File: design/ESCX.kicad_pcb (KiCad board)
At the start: 4 copper layers, 100 x 90 mm, 138 parts, among them J1 SWD, J2 Conn_Coaxial, J3 Screw_Terminal_01x02, J4 Screw_Terminal_01x03, J5 HALL_ENC, J6 USB_C_Receptacle_USB2.0_16P, Q1 IRF7854, Q2 IRF7854, Q3 IRF7854, Q4 IRF7854, Q5 IRF7854, Q6 IRF7854, SW1 SENSOR_VOLTAGE, U1 STM32F40X_LQFP64, U2 LM3671, U3 DRV8301, U4 nRF24L01P, U5 AD8418, U6 AD8418, U7 AD8418, X1 8MHz, X2 16MHz

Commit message: Correccion de DRC
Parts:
- J2: footprint Connector_Coaxial:SMA_Amphenol_901-143_Horizontal -> Connector_Coaxial:SMA_Amphenol_901-144_Vertical
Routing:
- net +3.3V: track 121.7 -> 116.0 mm

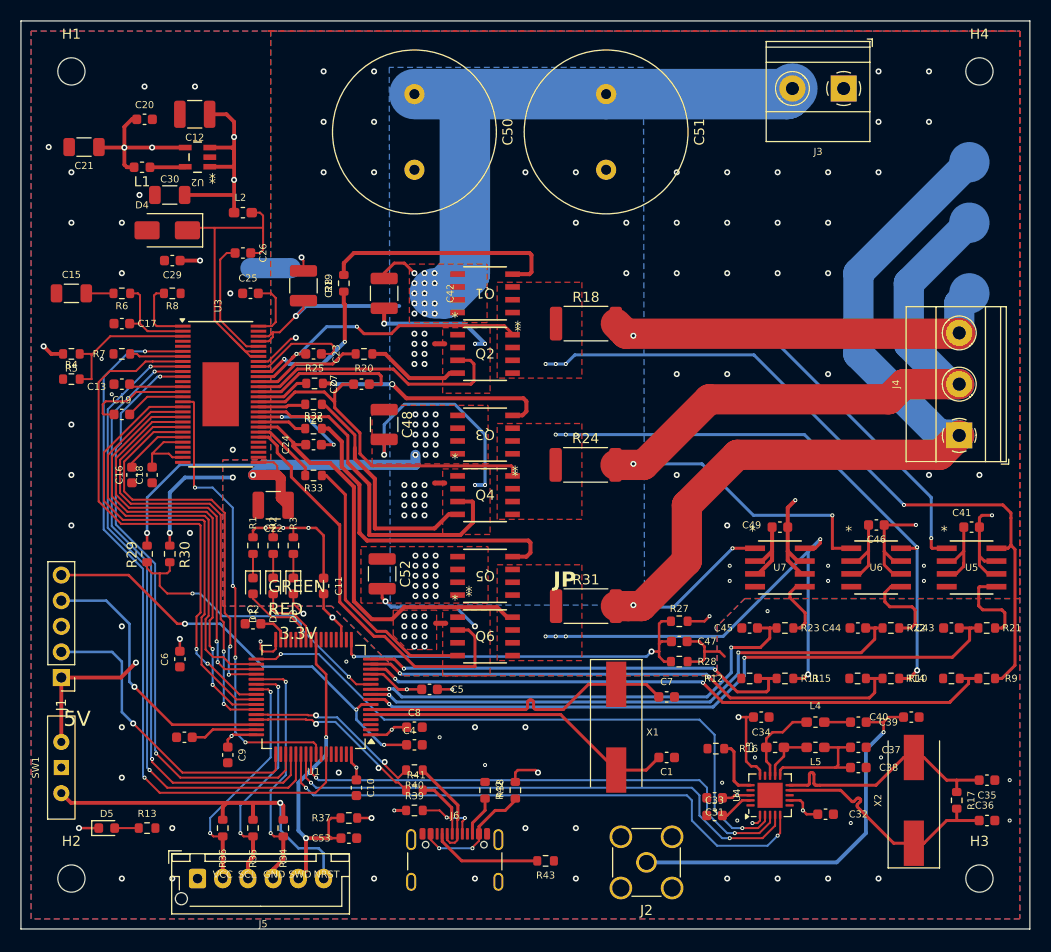
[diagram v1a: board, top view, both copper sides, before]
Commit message: reubicacion de designadores de Silkscreen
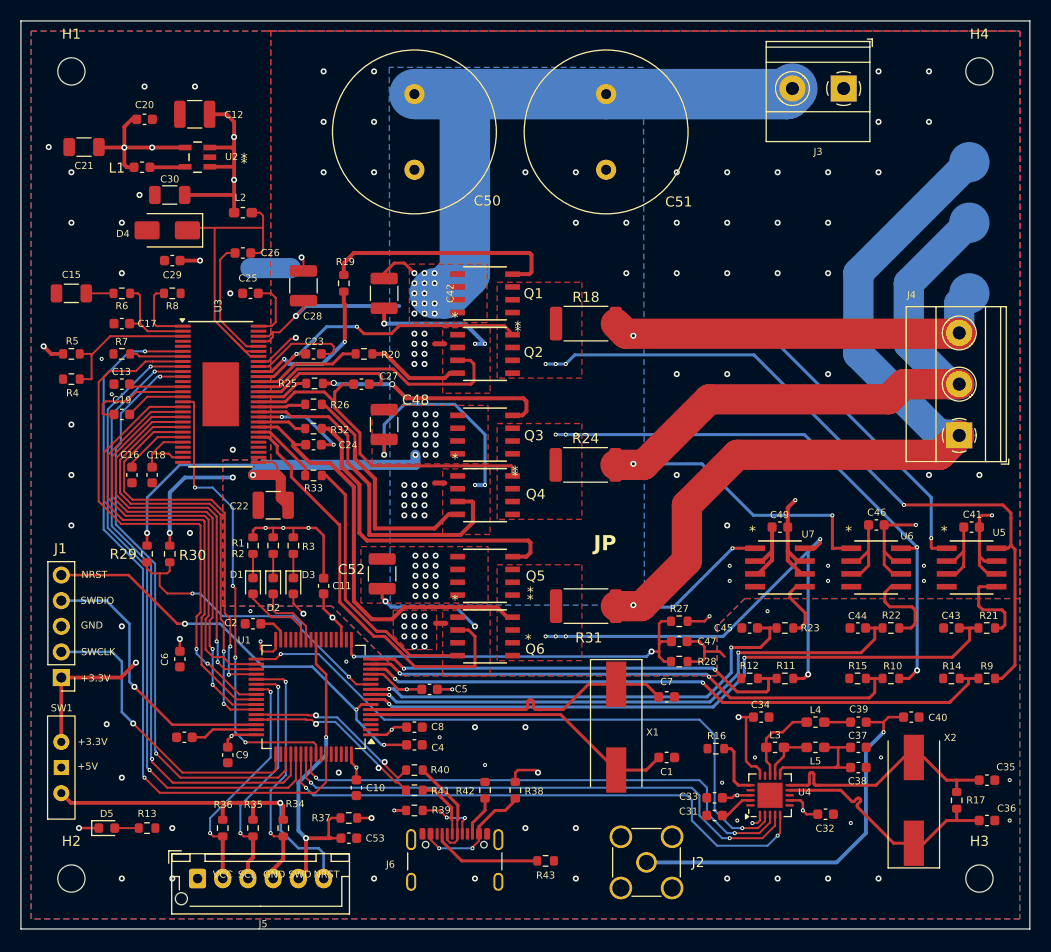
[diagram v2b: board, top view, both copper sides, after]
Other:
- board text added: "+3.3V"
- board text added: "+5V"
- board text added: "SWCLK"
- board text added: "SWDIO"
- board text removed: "3.3V"
- board text removed: "5V"
- board text removed: "GREEN"
- board text removed: "RED"

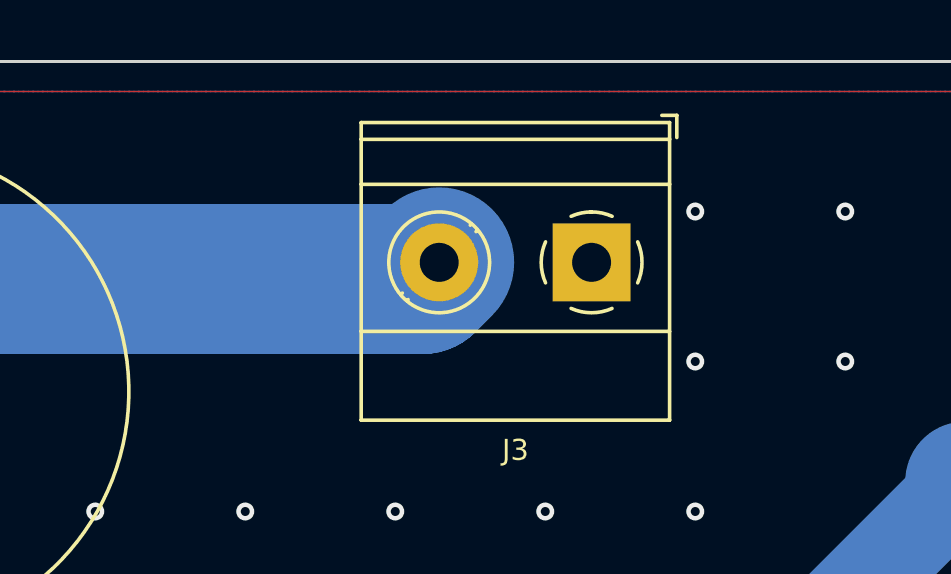
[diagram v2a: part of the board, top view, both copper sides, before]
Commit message: Agrego texto con +supply
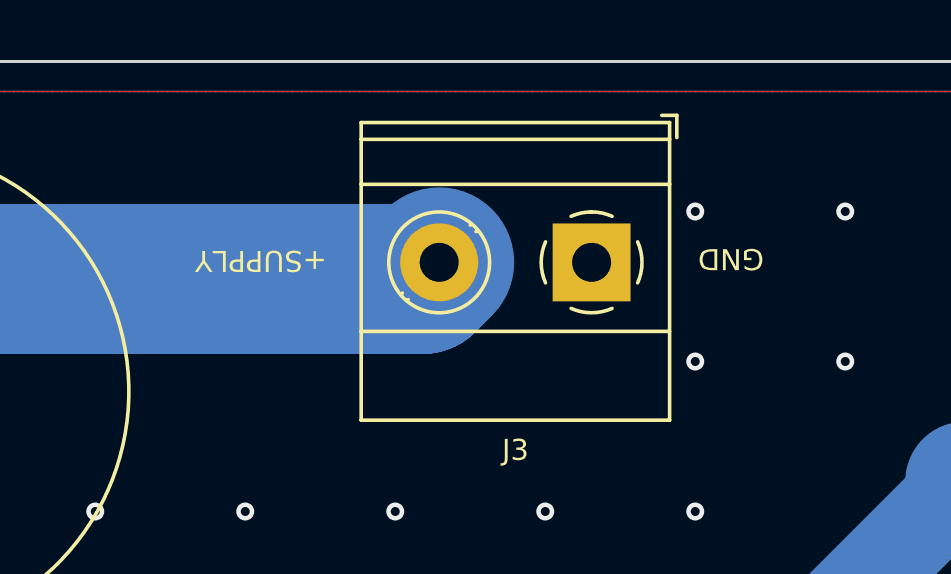
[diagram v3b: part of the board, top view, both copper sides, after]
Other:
- board text added: "+SUPPLY"
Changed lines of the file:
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@@
+		)
+	)
+	(gr_text "GND"
+		(at 185.19 50.58 180)
+		(layer "F.SilkS")
+		(effects
+			(font
+				(size 0.7 0.7)
+				(thickness 0.1)
+			)
 		)
 	)
@@
 		(layer "F.SilkS")
 		(effects
+			(font
+				(size 0.7 0.7)
+				(thickness 0.1)
+			)
+		)
+	)
+	(gr_text "+SUPPLY"
+		(at 169.52 50.64 180)
+		(layer "F.SilkS")
+		(effects

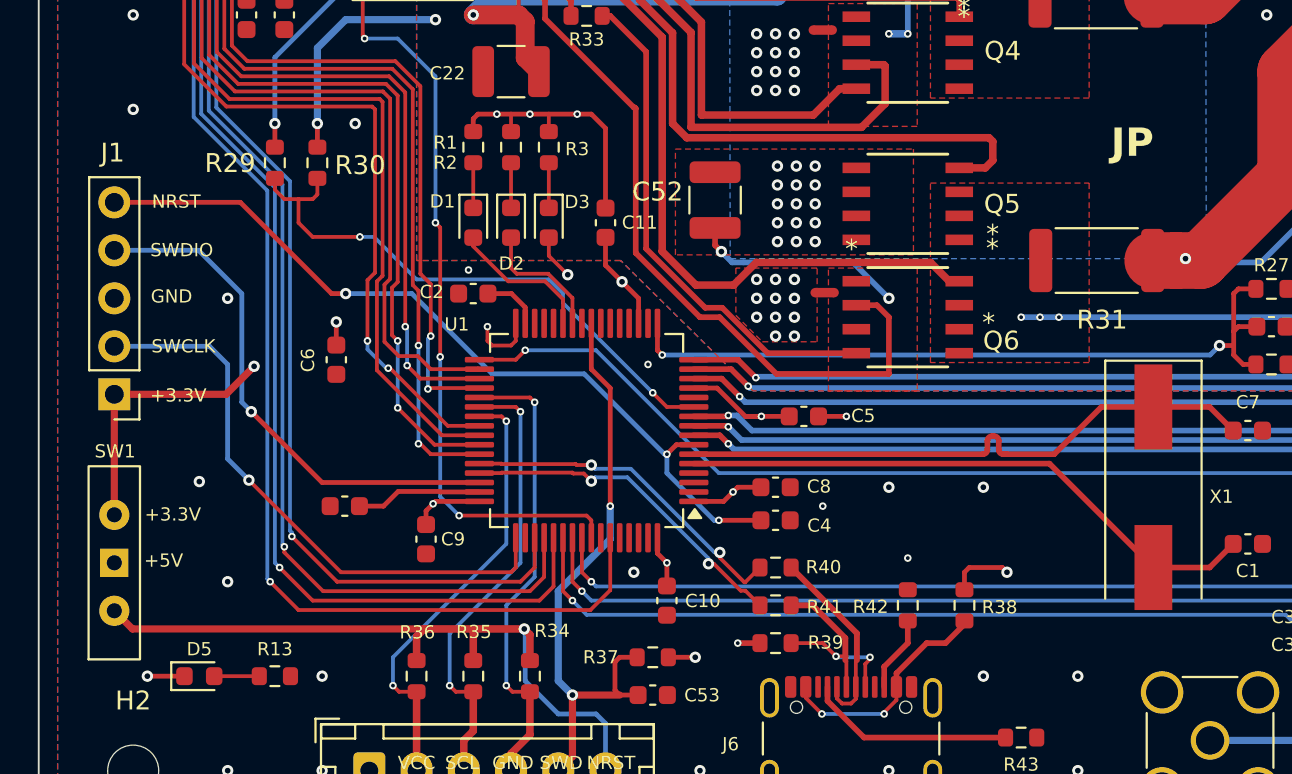
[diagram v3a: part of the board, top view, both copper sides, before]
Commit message: Cambio de switch de tension del sensor por jumper
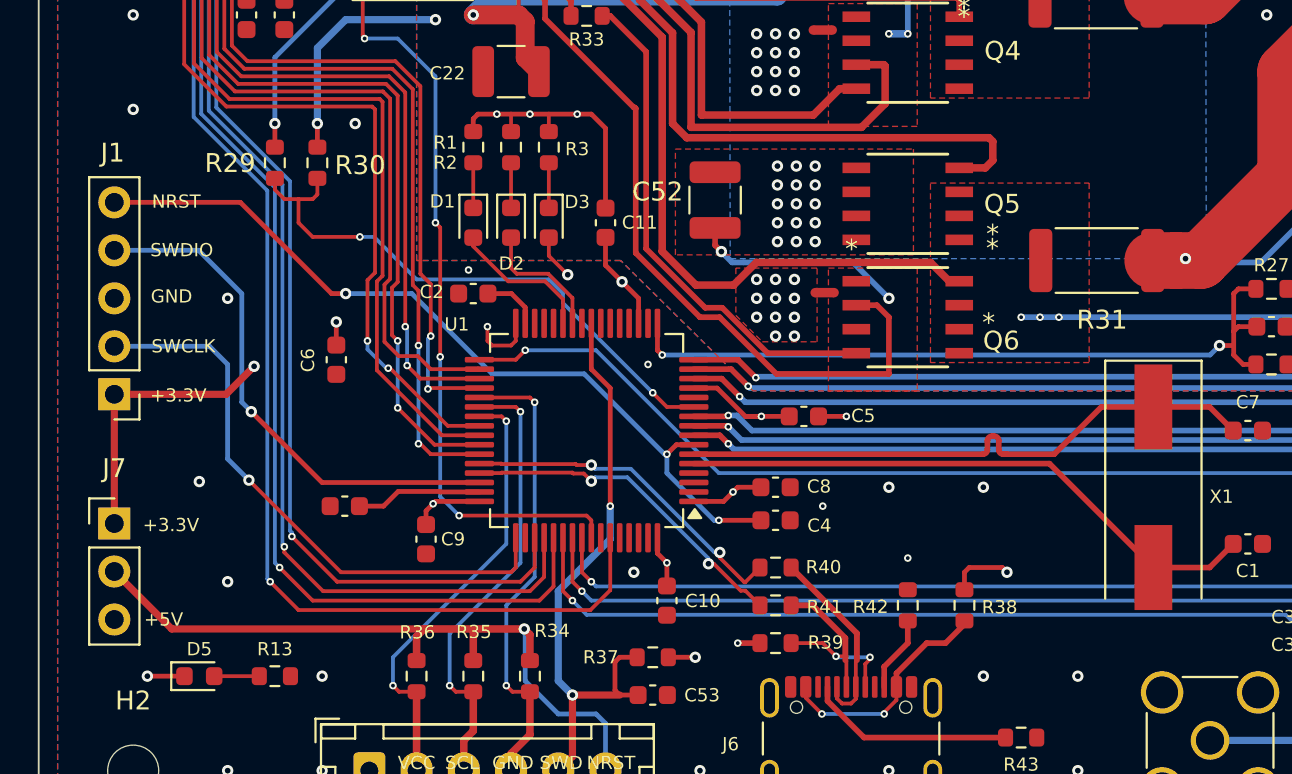
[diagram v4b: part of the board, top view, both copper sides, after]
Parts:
- removed SW1: SENSOR_VOLTAGE, Button_Switch_THT:SW_Slide-03_Wuerth-WS-SLTV_10x2.5x6.4_P2.54mm
- added J7: Sensor Voltage Switch, Connector_PinHeader_2.54mm:PinHeader_1x03_P2.54mm_Vertical, F.Cu at (103.0, 115.9)
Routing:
- net Net-(J5-Pin_6): track 37.9 -> 38.7 mm

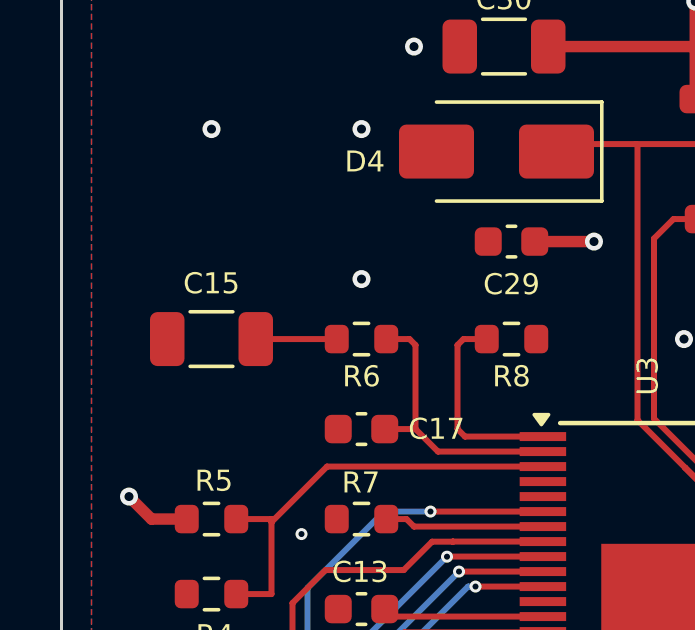
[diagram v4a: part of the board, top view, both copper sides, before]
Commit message: Abaratando costos
Cambios en numeros de jlcpcb, pasados a componentes básicos
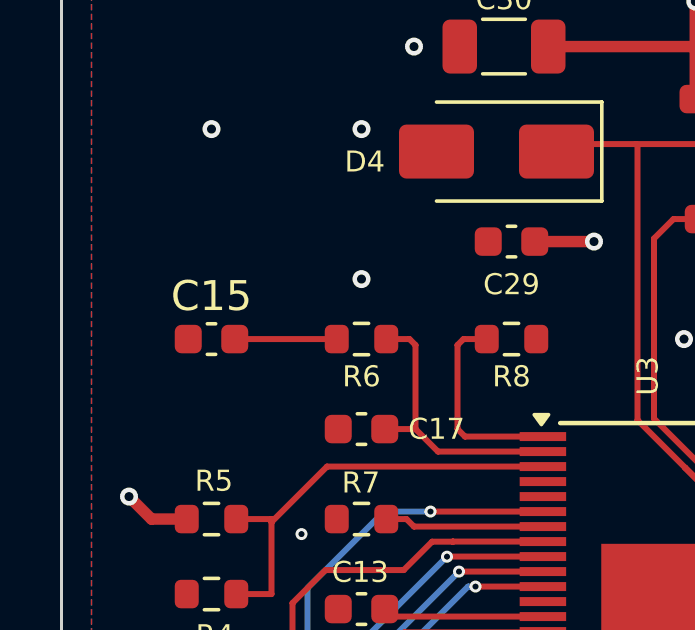
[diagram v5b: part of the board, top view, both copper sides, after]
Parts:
- C15: footprint Capacitor_SMD:C_1206_3216Metric -> Capacitor_SMD:C_0603_1608Metric
- D1: value Red LED -> R2
- D2: value Green LED -> G1
- D3: value Blue LED -> B3
- D5: value Red LED -> R4
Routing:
- net Net-(C15-Pad2): track 2.70 -> 3.40 mm

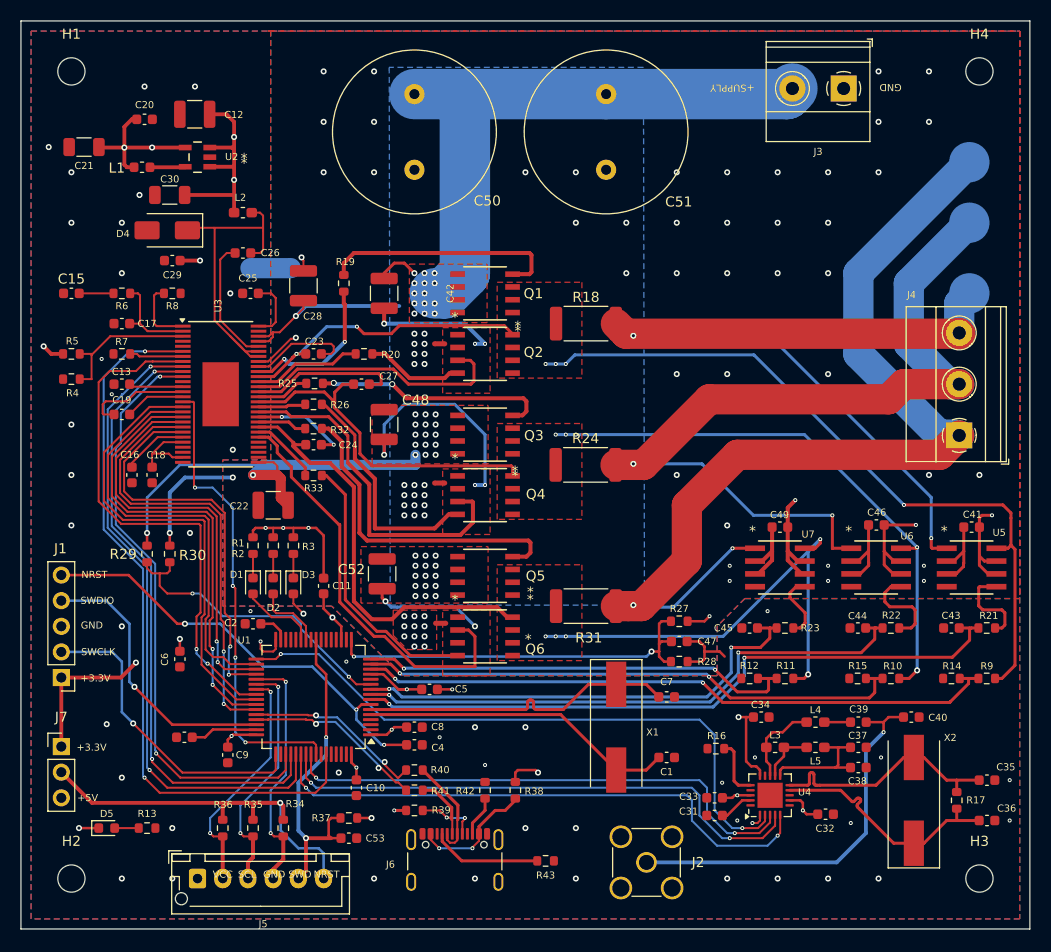
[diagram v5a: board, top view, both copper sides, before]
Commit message: Sacado de NRF
Sacado de NRF, re-hecho constraints
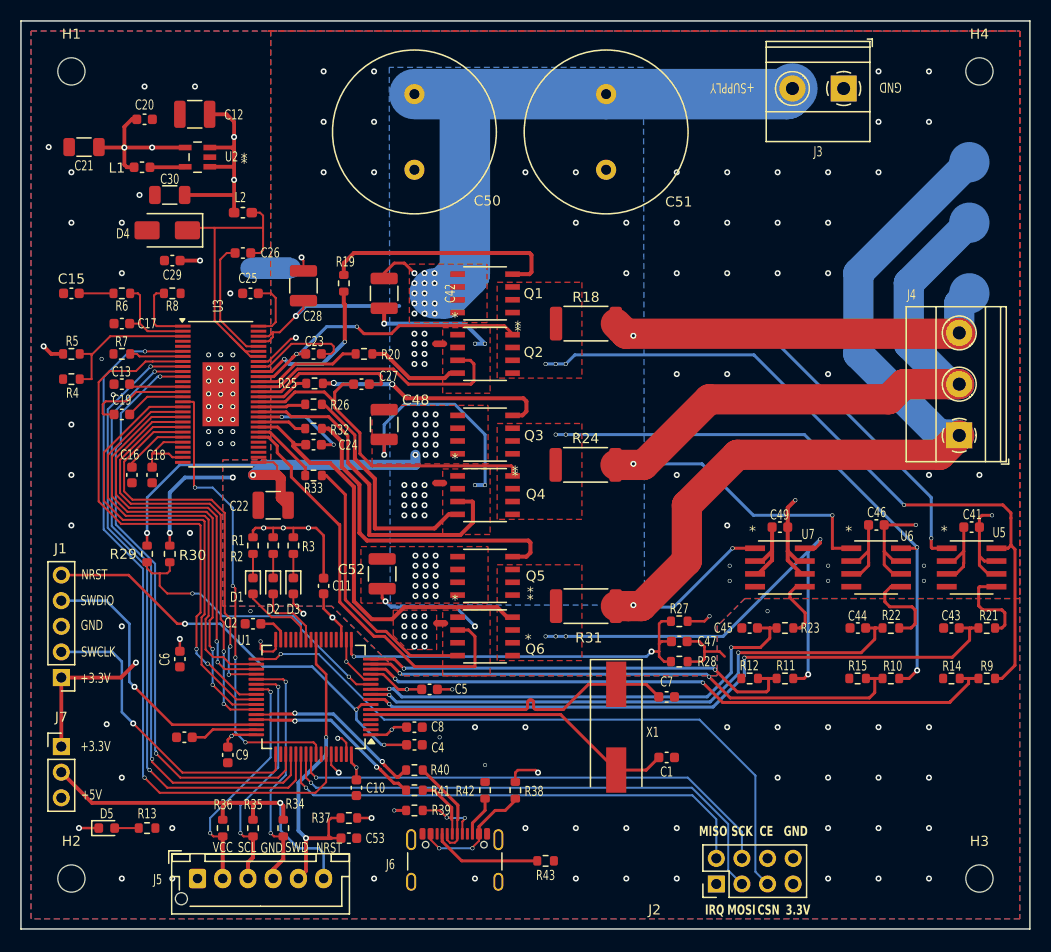
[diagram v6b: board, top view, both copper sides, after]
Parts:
- removed C31, C32, C33, C34: 100nF, Capacitor_SMD:C_0603_1608Metric
- removed C35, C36: 22pF, Capacitor_SMD:C_0603_1608Metric
- removed C37: 2.2nF, Capacitor_SMD:C_0603_1608Metric
- removed C38: 4.7pF, Capacitor_SMD:C_0603_1608Metric
- removed C39: 1.5pF, Capacitor_SMD:C_0603_1608Metric
- removed C40: 1pF, Capacitor_SMD:C_0603_1608Metric
- removed L3: 8.2n, Inductor_SMD:L_0603_1608Metric_Pad1.05x0.95mm_HandSolder
- removed L4: 3.9n, Inductor_SMD:L_0603_1608Metric_Pad1.05x0.95mm_HandSolder
- removed L5: 2.7n, Inductor_SMD:L_0603_1608Metric_Pad1.05x0.95mm_HandSolder
- removed R16: 22kΩ, Resistor_SMD:R_0603_1608Metric
- removed R17: 1MΩ, Resistor_SMD:R_0603_1608Metric
- removed U4: nRF24L01P, Package_DFN_QFN:QFN-20-1EP_4x4mm_P0.5mm_EP2.5x2.5mm
- removed X2: 16MHz, Crystal:Crystal_SMD_HC49-SD
- J2: value Conn_Coaxial -> Conn_02x04_Top_Bottom; footprint Connector_Coaxial:SMA_Amphenol_901-144_Vertical -> Connector_PinHeader_2.54mm:PinHeader_2x04_P2.54mm_Vertical
- moved J2 7.24 mm to (167.9, 129.5), turned to 90 degrees
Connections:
- J2 pad 1: Net-(J2-In) -> /NRF/IRQ
- J2 pad 2: GND1 -> /MCU/PD2
- J6 pad A6: /USB_Interface/dusb+ -> Net-(J6-D+-PadA6)
- J6 pad A7: /USB_Interface/dusb- -> Net-(J6-D--PadA7)
- J6 pad B6: /USB_Interface/dusb+ -> Net-(J6-D+-PadA6)
- J6 pad B7: /USB_Interface/dusb- -> Net-(J6-D--PadA7)
- R39 pad 2: /USB_Interface/dusb+ -> Net-(J6-D+-PadA6)
- R40 pad 1: /MCU/USB_DN -> /USB_Interface/dusb-
- R40 pad 2: /USB_Interface/dusb- -> Net-(J6-D--PadA7)
- R41 pad 1: /MCU/USB_DP -> /USB_Interface/dusb+
- R41 pad 2: /USB_Interface/dusb+ -> Net-(J6-D+-PadA6)
- U1 pad 44: /MCU/USB_DN -> /USB_Interface/dusb-
- U1 pad 45: /MCU/USB_DP -> /USB_Interface/dusb+
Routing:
- net Net-(J2-In): track 38.8 -> 0.00 mm, vias 1 -> 0
- net Net-(U4-XC2): track 24.2 -> 0.00 mm
- net Net-(U4-XC1): track 24.2 -> 0.00 mm
- net /MCU/USB_DP: track 18.1 -> 0.00 mm, vias 2 -> 0
- net /MCU/USB_DN: track 17.9 -> 0.00 mm, vias 2 -> 0
- net +3.3V: track 116.4 -> 100.2 mm, vias 22 -> 18
- net Net-(J6-D+-PadA6): track 0.00 -> 12.8 mm, vias 0 -> 2
- net Net-(U4-VDD_PA): track 12.3 -> 0.00 mm
- net Net-(J6-D--PadA7): track 0.00 -> 10.2 mm
- net GND1: track 40.2 -> 50.1 mm, vias 51 -> 83
- net Net-(U4-ANT2): track 8.52 -> 0.00 mm
- net /USB_Interface/dusb-: track 10.2 -> 17.9 mm, vias 0 -> 2
- net /MCU/PD2: track 56.4 -> 49.4 mm, vias 2 -> 1
- net Net-(U4-IREF): track 5.81 -> 0.00 mm
- net Net-(U4-ANT1): track 5.42 -> 0.00 mm
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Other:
- board text added: "3.3V"
- board text added: "CE"
- board text added: "CSN"
- board text added: "IRQ"
- board text added: "MISO"
- board text added: "MOSI"
- board text added: "SCK"
